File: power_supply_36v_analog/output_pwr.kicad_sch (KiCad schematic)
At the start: 4 parts, among them J501 OUTPUT

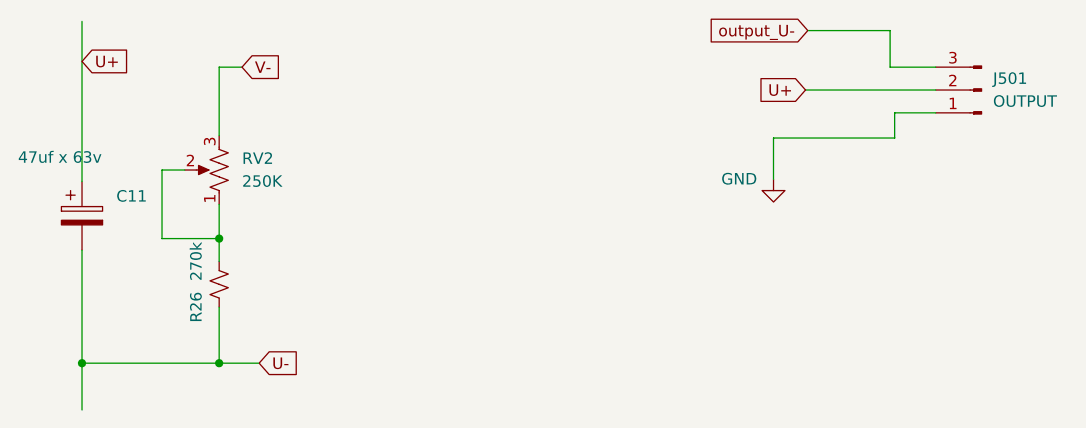
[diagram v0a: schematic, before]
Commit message: Convert global labels to hierarchical pins in all schematic sheets
- control_driver.kicad_sch: US-, output_U-, to_base_driver_adjust, NODO_001, U-
- pwr_driver_output.kicad_sch: AMPERIMETRO+, to_base_driver_adjust, NODO_001, U+
- output_pwr.kicad_sch: U+, V-, U-, output_U-
- power_supply_36v.kicad_sch: TR21, +36V, TR11, TR12, TR22, -36V
- Added corresponding pins to sheet symbols in root schematic
- Updated .gitignore to exclude .history and .lck files
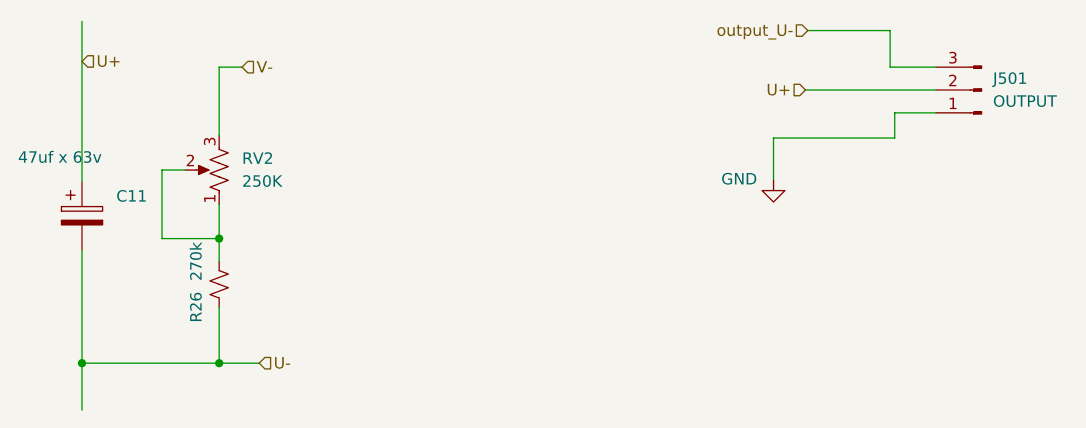
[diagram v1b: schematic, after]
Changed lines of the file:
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@@
     (stroke (width 0) (type default))
   )
-  (global_label "U+" (shape input) (at 108.585 76.835 0) (fields_autoplaced)
-    (effects (font (size 1.27 1.27)) (justify left))
-    (property "Intersheetrefs" "${INTERSHEET_REFS}" (at 114.3937 76.835 0)
-      (effects (font (size 1.27 1.27)) (justify left) hide)
-    )
-  )
-  (global_label "U+" (shape input) (at 188.976 80.01 180) (fields_autoplaced)
-    (effects (font (size 1.27 1.27)) (justify right))
-    (property "Intersheetrefs" "${INTERSHEET_REFS}" (at 183.1673 80.01 0)
-      (effects (font (size 1.27 1.27)) (justify right) hide)
-    )
-  )
-  (global_label "V-" (shape input) (at 126.365 77.47 0) (fields_autoplaced)
-    (effects (font (size 1.27 1.27)) (justify left))
-    (property "Intersheetrefs" "${INTERSHEET_REFS}" (at 131.9318 77.47 0)
-      (effects (font (size 1.27 1.27)) (justify left) hide)
-    )
-  )
-  (global_label "U-" (shape input) (at 128.27 110.363 0) (fields_autoplaced)
-    (effects (font (size 1.27 1.27)) (justify left))
-    (property "Intersheetrefs" "${INTERSHEET_REFS}" (at 134.0787 110.363 0)
-      (effects (font (size 1.27 1.27)) (justify left) hide)
-    )
-  )
-  (global_label "output_U-" (shape input) (at 189.23 73.406 180) (fields_autoplaced)
-    (effects (font (size 1.27 1.27)) (justify right))
-    (property "Intersheetrefs" "${INTERSHEET_REFS}" (at 176.4063 73.406 0)
-      (effects (font (size 1.27 1.27)) (justify right) hide)
-    )
-  )
+  (hierarchical_label "U+" (shape input) (at 108.585 76.835 0) (effects (font (size 1.27 1.27))))
+  (hierarchical_label "U+" (shape input) (at 188.976 80.01 180) (effects (font (size 1.27 1.27))))
+  (hierarchical_label "V-" (shape input) (at 126.365 77.47 0) (effects (font (size 1.27 1.27))))
+  (hierarchical_label "U-" (shape input) (at 128.27 110.363 0) (effects (font (size 1.27 1.27))))
+  (hierarchical_label "output_U-" (shape input) (at 189.23 73.406 180) (effects (font (size 1.27 1.27))))
   (netclass_flag "" (length 2.54) (shape round) (at 108.585 115.57 180) (fields_autoplaced)
     (effects (font (size 1.27 1.27)) (justify right bottom))

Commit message: Fix pin spacing to 2.54mm like DiscoveryAnalog3 sheet
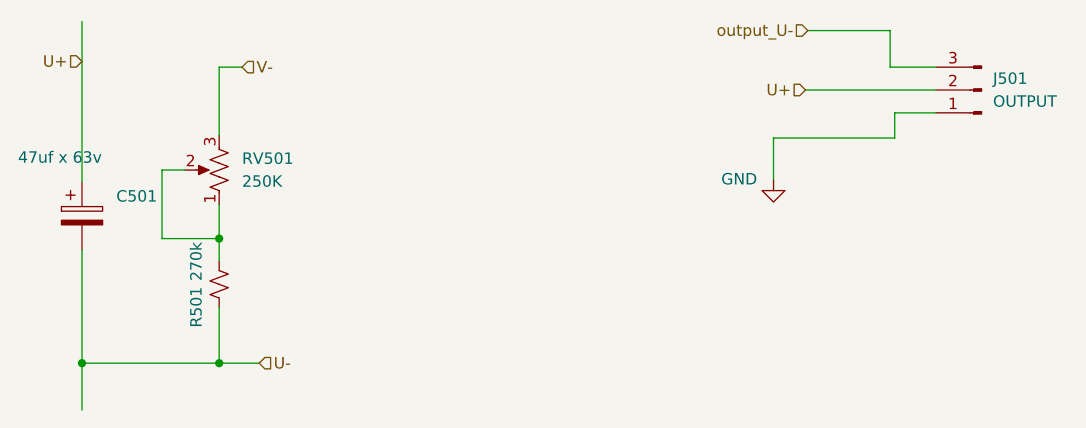
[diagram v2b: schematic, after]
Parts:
- renumbered C11 to C501, R26 to R501, RV2 to RV501
